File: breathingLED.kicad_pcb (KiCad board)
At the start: 2 copper layers, 37 x 37 mm, 18 parts, among them Q1 Q_PMOS_GSD, Q2 BC847BLT1G, Q3 BC847BLT1G, SW1 SW_SPDT

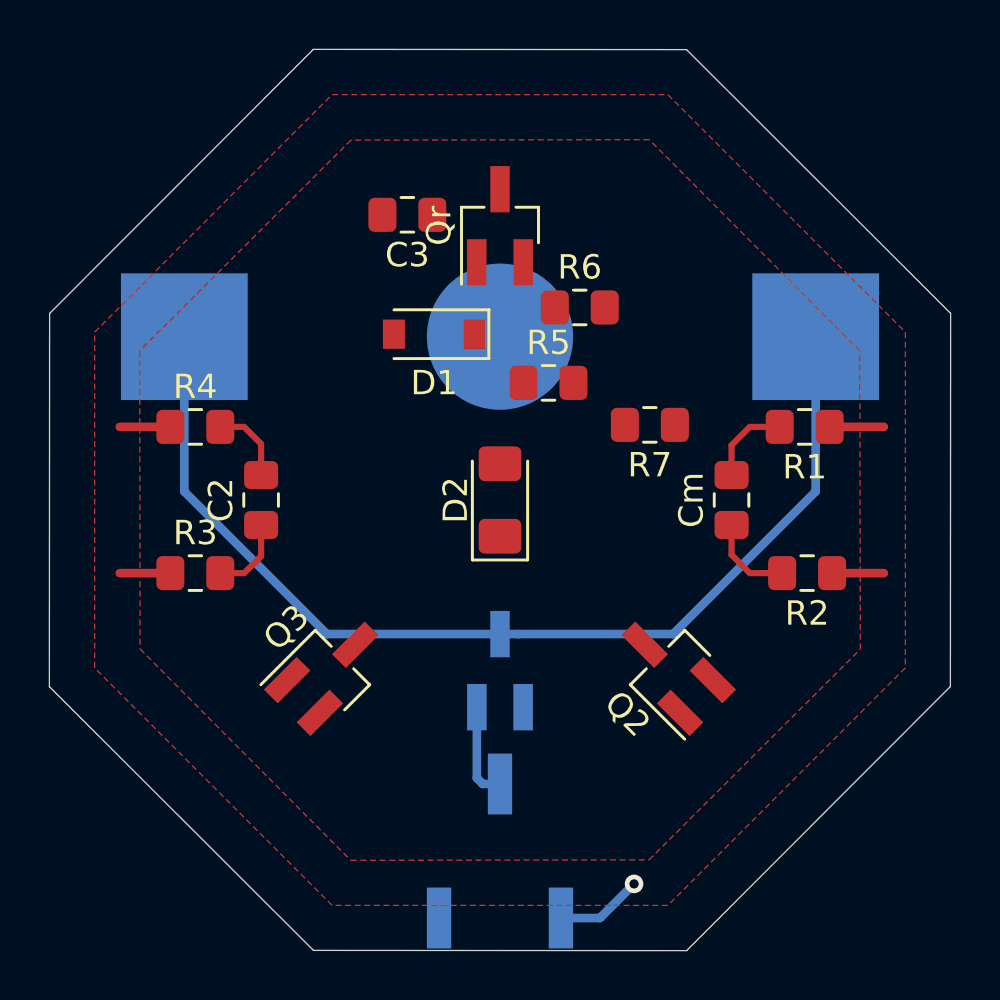
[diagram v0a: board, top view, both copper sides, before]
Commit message: Routing complete
Finished routing PCB with small copper plane near centre for ground
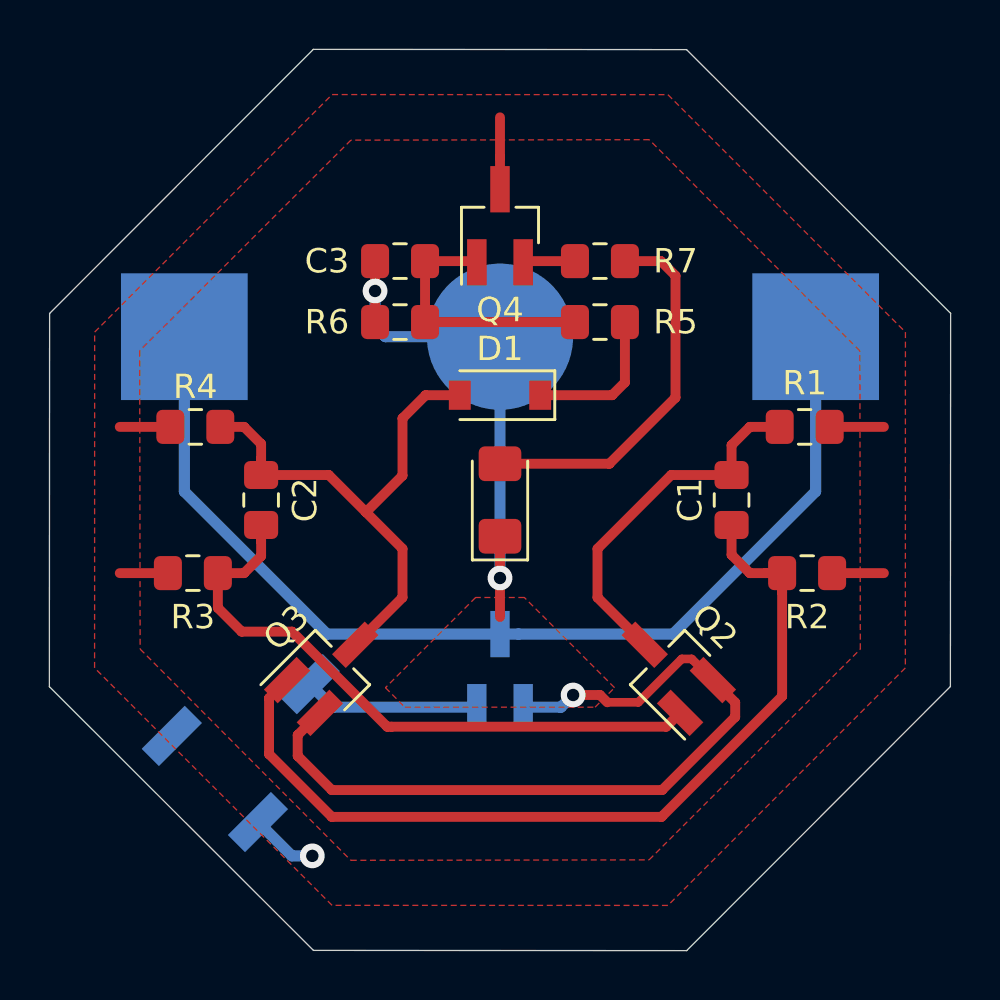
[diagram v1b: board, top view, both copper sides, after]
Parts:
- removed D2: GREEN, LED_SMD:LED_1206_3216Metric_Pad1.42x1.75mm_HandSolder
- added LED: GREEN, LED_SMD:LED_1206_3216Metric_Pad1.42x1.75mm_HandSolder, F.Cu at (100.0, 100.0)
- moved SW1 10.9 mm to (90.2, 109.5), turned to 135 degrees
- moved R6 7.40 mm to (95.9, 92.7), turned to 180 degrees
- moved R7 7.02 mm to (104.1, 90.2), turned to 0 degrees
- moved D1 3.68 mm to (100.0, 95.7)
- moved R5 3.27 mm to (104.1, 92.7), turned to 180 degrees
- moved C3 1.92 mm to (95.9, 90.2), turned to 0 degrees
- moved R3 0.10 mm to (87.4, 103.0)
- renumbered Cm to C1, Qr to Q4
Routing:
- net GND: track 0.00 -> 55.5 mm, vias 0 -> 3
- net Net-(C1-Pad1): track 3.61 -> 36.2 mm
- net Net-(C2-Pad1): track 3.24 -> 26.0 mm
- net Net-(C2-Pad2): track 3.24 -> 22.3 mm
- net Net-(D2-Pad2): track 0.00 -> 15.6 mm
- net Net-(C1-Pad2): track 3.51 -> 15.0 mm
- net Net-(C3-Pad2): track 0.00 -> 10.8 mm
- net Net-(D1-Pad1): track 0.00 -> 6.27 mm
- net Net-(Q1-Pad2): track 3.96 -> 7.25 mm
- net +3V0: track 12.1 -> 14.3 mm
- net Net-(Q4-Pad2): track 0.00 -> 2.15 mm
- added copper zone on F.Cu, net GND
